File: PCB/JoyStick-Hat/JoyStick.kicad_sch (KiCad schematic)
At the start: 0 parts

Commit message: LED drivers and Joystick
Finished LED driver scheamtics, corrected some problems with symbols. added conenctors for joystick and buttons, connected RPI pins to MCU
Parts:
- added J4, J5: Conn_01x03_Pin, symbol Connector:Conn_01x03_Pin
- added J6: Conn_01x04_Pin, symbol Connector:Conn_01x04_Pin
- added J7, J8: Conn_01x02_Pin, symbol Connector:Conn_01x02_Pin
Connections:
- new net +3.3V: J4.3 (Pin_3), J5.3 (Pin_3)
- new net GND: J4.1 (Pin_1), J5.1 (Pin_1)
- new net JOYSTICK_X: J5.2 (Pin_2)
- new net JOYSTICK_Y: J4.2 (Pin_2)
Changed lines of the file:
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@@
 (kicad_sch (version 20230121) (generator eeschema)
   (paper "A4")
+  (wire (pts (xy 44.45 113.03) (xy 102.87 113.03))
+    (stroke (width 0) (type default))
+  )
+  (wire (pts (xy 102.87 115.57) (xy 102.87 124.46))
+    (stroke (width 0) (type default))
+  )
+  (wire (pts (xy 44.45 80.01) (xy 102.87 80.01))
+    (stroke (width 0) (type default))
+  )
+  (wire (pts (xy 102.87 68.58) (xy 102.87 77.47))
+    (stroke (width 0) (type default))
+  )
+  (wire (pts (xy 102.87 82.55) (xy 102.87 88.9))
+    (stroke (width 0) (type default))
+  )
+  (wire (pts (xy 102.87 102.87) (xy 102.87 110.49))
+    (stroke (width 0) (type default))
+  )
+  (hierarchical_label "JOYSTICK_X" (shape input) (at 44.45 80.01 180) (fields_autoplaced)
+    (effects (font (size 1.27 1.27)) (justify right))
+  )
+  (hierarchical_label "JOYSTICK_Y" (shape input) (at 44.45 113.03 180) (fields_autoplaced)
+    (effects (font (size 1.27 1.27)) (justify right))
+  )
+  (symbol (lib_id "Connector:Conn_01x02_Pin") (at 171.45 101.6 0) (unit 1)
+    (in_bom yes) (on_board yes) (dnp no)
+    (property "Reference" "J7" (at 172.72 99.06 0)
+      (effects (font (size 1.27 1.27)))
+    )
+    (property "Value" "Conn_01x02_Pin" (at 179.07 106.68 0)
+      (effects (font (size 1.27 1.27)))
+    )
+    (property "Footprint" "" (at 171.45 101.6 0)
+      (effects (font (size 1.27 1.27)) hide)
+    )
+    (property "Datasheet" "~" (at 171.45 101.6 0)
+      (effects (font (size 1.27 1.27)) hide)
+    )
+    (pin "1")
+    (pin "2")
+    (instances
+      (project "JoyStick-Hat"
+        (path "/cf0c81b5-5bdf-47c3-83c0-f6980f515e65/657fac1d-f0e2-4536-8020-58a2ff4b82f6"
+          (reference "J7") (unit 1)
+        )
+      )
+    )
+  )
+  (symbol (lib_id "Connector:Conn_01x02_Pin") (at 171.45 121.92 0) (unit 1)
+    (in_bom yes) (on_board yes) (dnp no)
+    (property "Reference" "J8" (at 172.72 119.38 0)
+      (effects (font (size 1.27 1.27)))
+    )
+    (property "Value" "Conn_01x02_Pin" (at 179.07 127 0)
+      (effects (font (size 1.27 1.27)))
+    )
+    (property "Footprint" "" (at 171.45 121.92 0)
+      (effects (font (size 1.27 1.27)) hide)
+    )
+    (property "Datasheet" "~" (at 171.45 121.92 0)
+      (effects (font (size 1.27 1.27)) hide)
+    )
+    (pin "1")
+    (pin "2")
+    (instances
+      (project "JoyStick-Hat"
+        (path "/cf0c81b5-5bdf-47c3-83c0-f6980f515e65/657fac1d-f0e2-4536-8020-58a2ff4b82f6"
+          (reference "J8") (unit 1)
+        )
+      )
+    )
+  )
+  (symbol (lib_id "Connector:Conn_01x03_Pin") (at 107.95 80.01 180) (unit 1)
+    (in_bom yes) (on_board yes) (dnp no) (fields_autoplaced)
+    (property "Reference" "J5" (at 109.22 78.74 0)
+      (effects (font (size 1.27 1.27)) (justify right))
+    )
+    (property "Value" "Conn_01x03_Pin" (at 109.22 81.28 0)
+      (effects (font (size 1.27 1.27)) (justify right))
+    )
+    (property "Footprint" "" (at 107.95 80.01 0)
+      (effects (font (size 1.27 1.27)) hide)
+    )
+    (property "Datasheet" "~" (at 107.95 80.01 0)
+      (effects (font (size 1.27 1.27)) hide)
+    )
+    (pin "1")
+    (pin "2")
+    (pin "3")
+    (instances
+      (project "JoyStick-Hat"
+        (path "/cf0c81b5-5bdf-47c3-83c0-f6980f515e65/657fac1d-f0e2-4536-8020-58a2ff4b82f6"
+          (reference "J5") (unit 1)
+        )
+      )
+    )
+  )
+  (symbol (lib_id "Connector:Conn_01x03_Pin") (at 107.95 113.03 180) (unit 1)
+    (in_bom yes) (on_board yes) (dnp no) (fields_autoplaced)
+    (property "Reference" "J4" (at 109.22 111.76 0)
+      (effects (font (size 1.27 1.27)) (justify right))
+    )
+    (property "Value" "Conn_01x03_Pin" (at 109.22 114.3 0)
+      (effects (font (size 1.27 1.27)) (justify right))
+    )
+    (property "Footprint" "" (at 107.95 113.03 0)
+      (effects (font (size 1.27 1.27)) hide)
+    )
+    (property "Datasheet" "~" (at 107.95 113.03 0)
+      (effects (font (size 1.27 1.27)) hide)
+    )
+    (pin "1")
+    (pin "2")
+    (pin "3")
+    (instances
+      (project "JoyStick-Hat"
+        (path "/cf0c81b5-5bdf-47c3-83c0-f6980f515e65/657fac1d-f0e2-4536-8020-58a2ff4b82f6"
+          (reference "J4") (unit 1)
+        )
+      )
+    )
+  )
+  (symbol (lib_id "power:GND") (at 102.87 124.46 0) (unit 1)
+    (in_bom yes) (on_board yes) (dnp no) (fields_autoplaced)
+    (property "Reference" "#PWR040" (at 102.87 130.81 0)
+      (effects (font (size 1.27 1.27)) hide)
+    )
+    (property "Value" "GND" (at 102.87 129.54 0)
+      (effects (font (size 1.27 1.27)))
+    )
+    (property "Footprint" "" (at 102.87 124.46 0)
+      (effects (font (size 1.27 1.27)) hide)
+    )
+    (property "Datasheet" "" (at 102.87 124.46 0)
+      (effects (font (size 1.27 1.27)) hide)
+    )
+    (pin "1")
+    (instances
+      (project "JoyStick-Hat"
+        (path "/cf0c81b5-5bdf-47c3-83c0-f6980f515e65/657fac1d-f0e2-4536-8020-58a2ff4b82f6"
+          (reference "#PWR040") (unit 1)
+        )
+      )
+    )
+  )
+  (symbol (lib_id "power:+3.3V") (at 102.87 102.87 0) (unit 1)
+    (in_bom yes) (on_board yes) (dnp no) (fields_autoplaced)
+    (property "Reference" "#PWR041" (at 102.87 106.68 0)
+      (effects (font (size 1.27 1.27)) hide)
+    )
+    (property "Value" "+3.3V" (at 102.87 97.79 0)
+      (effects (font (size 1.27 1.27)))
+    )
+    (property "Footprint" "" (at 102.87 102.87 0)
+      (effects (font (size 1.27 1.27)) hide)
+    )
+    (property "Datasheet" "" (at 102.87 102.87 0)
+      (effects (font (size 1.27 1.27)) hide)
+    )
+    (pin "1")
+    (instances
+      (project "JoyStick-Hat"
+        (path "/cf0c81b5-5bdf-47c3-83c0-f6980f515e65/657fac1d-f0e2-4536-8020-58a2ff4b82f6"
+          (reference "#PWR041") (unit 1)
+        )
+      )
+    )
+  )
+  (symbol (lib_id "Connector:Conn_01x04_Pin") (at 170.18 80.01 0) (unit 1)
+    (in_bom yes) (on_board yes) (dnp no)
+    (property "Reference" "J6" (at 170.18 74.93 0)
+      (effects (font (size 1.27 1.27)))
+    )
+    (property "Value" "Conn_01x04_Pin" (at 177.8 87.63 0)
+      (effects (font (size 1.27 1.27)))
+    )
+    (property "Footprint" "" (at 170.18 80.01 0)
+      (effects (font (size 1.27 1.27)) hide)
+    )
+    (property "Datasheet" "~" (at 170.18 80.01 0)
+      (effects (font (size 1.27 1.27)) hide)
+    )
+    (pin "1")
+    (pin "2")
+    (pin "3")
+    (pin "4")
+    (instances
+      (project "JoyStick-Hat"
+        (path "/cf0c81b5-5bdf-47c3-83c0-f6980f515e65/657fac1d-f0e2-4536-8020-58a2ff4b82f6"
+          (reference "J6") (unit 1)
+        )
+      )
+    )
+  )
+  (symbol (lib_id "power:GND") (at 102.87 88.9 0) (unit 1)
+    (in_bom yes) (on_board yes) (dnp no) (fields_autoplaced)
+    (property "Reference" "#PWR039" (at 102.87 95.25 0)
+      (effects (font (size 1.27 1.27)) hide)
+    )
+    (property "Value" "GND" (at 102.87 93.98 0)
+      (effects (font (size 1.27 1.27)))
+    )
+    (property "Footprint" "" (at 102.87 88.9 0)
+      (effects (font (size 1.27 1.27)) hide)
+    )
+    (property "Datasheet" "" (at 102.87 88.9 0)
+      (effects (font (size 1.27 1.27)) hide)
+    )
+    (pin "1")
+    (instances
+      (project "JoyStick-Hat"
+        (path "/cf0c81b5-5bdf-47c3-83c0-f6980f515e65/657fac1d-f0e2-4536-8020-58a2ff4b82f6"
+          (reference "#PWR039") (unit 1)
+        )
+      )
+    )
+  )
+  (symbol (lib_id "power:+3.3V") (at 102.87 68.58 0) (unit 1)
+    (in_bom yes) (on_board yes) (dnp no) (fields_autoplaced)
+    (property "Reference" "#PWR042" (at 102.87 72.39 0)
+      (effects (font (size 1.27 1.27)) hide)
+    )
+    (property "Value" "+3.3V" (at 102.87 63.5 0)
+      (effects (font (size 1.27 1.27)))
+    )
+    (property "Footprint" "" (at 102.87 68.58 0)
+      (effects (font (size 1.27 1.27)) hide)
+    )
+    (property "Datasheet" "" (at 102.87 68.58 0)
+      (effects (font (size 1.27 1.27)) hide)
+    )
+    (pin "1")
+    (instances
+      (project "JoyStick-Hat"
+        (path "/cf0c81b5-5bdf-47c3-83c0-f6980f515e65/657fac1d-f0e2-4536-8020-58a2ff4b82f6"
+          (reference "#PWR042") (unit 1)
+        )
+      )
+    )
+  )
 )

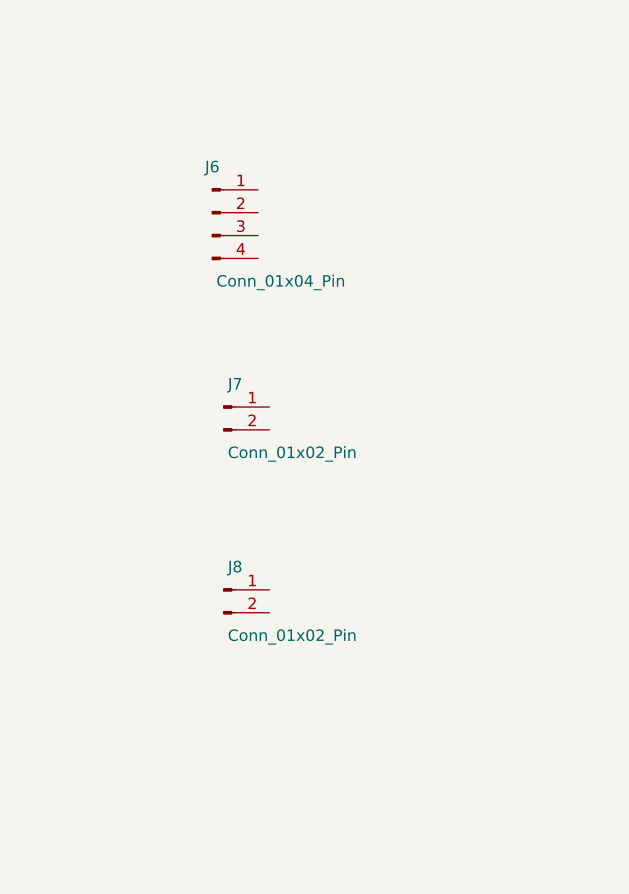
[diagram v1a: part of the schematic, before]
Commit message: Sheet Conenctivity and RS485
Added more sheet entries throughuot the project connecting different subsystems to the main MCU schematic. Also added  new sheet for the RS485 interface for communicating with the motor control board.
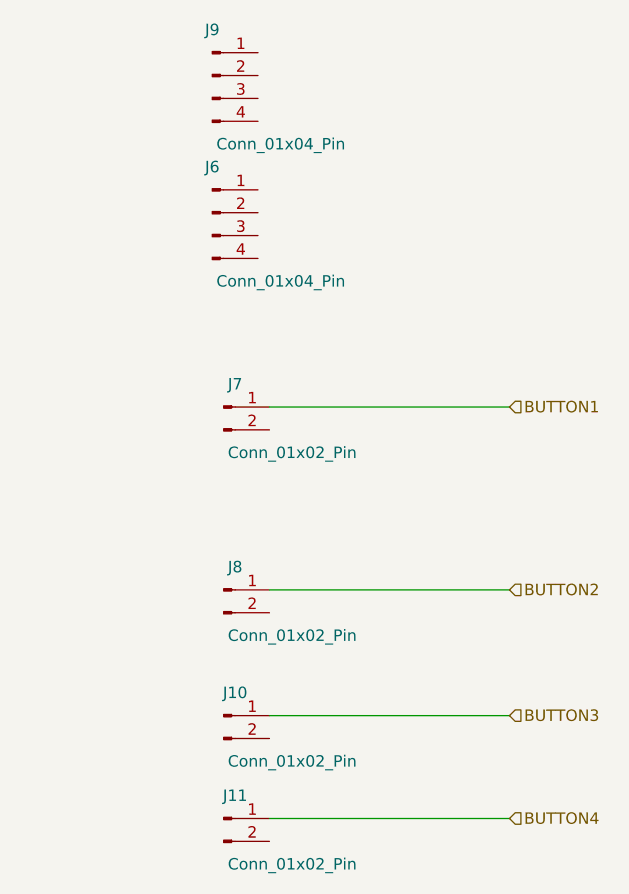
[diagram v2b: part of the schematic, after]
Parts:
- added J10, J11: Conn_01x02_Pin, symbol Connector:Conn_01x02_Pin
- added J9: Conn_01x04_Pin, symbol Connector:Conn_01x04_Pin
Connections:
- net BUTTON1: now reaches J7.1 (Pin_1)
- net BUTTON2: now reaches J8.1 (Pin_1)
- new net BUTTON3: J10.1 (Pin_1)
- new net BUTTON4: J11.1 (Pin_1)
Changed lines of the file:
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@@
 (kicad_sch (version 20230121) (generator eeschema)
   (paper "A4")
+  (wire (pts (xy 176.53 121.92) (xy 203.2 121.92))
+    (stroke (width 0) (type default))
+  )
   (wire (pts (xy 44.45 113.03) (xy 102.87 113.03))
     (stroke (width 0) (type default))
@@
     (stroke (width 0) (type default))
   )
+  (wire (pts (xy 176.53 101.6) (xy 203.2 101.6))
+    (stroke (width 0) (type default))
+  )
+  (wire (pts (xy 176.53 147.32) (xy 203.2 147.32))
+    (stroke (width 0) (type default))
+  )
   (wire (pts (xy 44.45 80.01) (xy 102.87 80.01))
     (stroke (width 0) (type default))
@@
   (wire (pts (xy 102.87 102.87) (xy 102.87 110.49))
     (stroke (width 0) (type default))
+  )
+  (wire (pts (xy 176.53 135.89) (xy 203.2 135.89))
+    (stroke (width 0) (type default))
+  )
+  (hierarchical_label "BUTTON3" (shape input) (at 203.2 135.89 0) (fields_autoplaced)
+    (effects (font (size 1.27 1.27)) (justify left))
+  )
+  (hierarchical_label "BUTTON2" (shape input) (at 203.2 121.92 0) (fields_autoplaced)
+    (effects (font (size 1.27 1.27)) (justify left))
   )
   (hierarchical_label "JOYSTICK_X" (shape input) (at 44.45 80.01 180) (fields_autoplaced)
@@
     (effects (font (size 1.27 1.27)) (justify right))
   )
+  (hierarchical_label "BUTTON1" (shape input) (at 203.2 101.6 0) (fields_autoplaced)
+    (effects (font (size 1.27 1.27)) (justify left))
+  )
+  (hierarchical_label "BUTTON4" (shape input) (at 203.2 147.32 0) (fields_autoplaced)
+    (effects (font (size 1.27 1.27)) (justify left))
+  )
   (symbol (lib_id "Connector:Conn_01x02_Pin") (at 171.45 101.6 0) (unit 1)
     (in_bom yes) (on_board yes) (dnp no)
@@
     )
   )
-  (symbol (lib_id "power:+3.3V") (at 102.87 102.87 0) (unit 1)
-    (in_bom yes) (on_board yes) (dnp no) (fields_autoplaced)
-    (property "Reference" "#PWR041" (at 102.87 106.68 0)
-      (effects (font (size 1.27 1.27)) hide)
-    )
-    (property "Value" "+3.3V" (at 102.87 97.79 0)
-      (effects (font (size 1.27 1.27)))
-    )
-    (property "Footprint" "" (at 102.87 102.87 0)
-      (effects (font (size 1.27 1.27)) hide)
-    )
-    (property "Datasheet" "" (at 102.87 102.87 0)
-      (effects (font (size 1.27 1.27)) hide)
-    )
-    (pin "1")
-    (instances
-      (project "JoyStick-Hat"
-        (path "/cf0c81b5-5bdf-47c3-83c0-f6980f515e65/657fac1d-f0e2-4536-8020-58a2ff4b82f6"
-          (reference "#PWR041") (unit 1)
-        )
-      )
-    )
-  )
-  (symbol (lib_id "Connector:Conn_01x04_Pin") (at 170.18 80.01 0) (unit 1)
-    (in_bom yes) (on_board yes) (dnp no)
-    (property "Reference" "J6" (at 170.18 74.93 0)
-      (effects (font (size 1.27 1.27)))
-    )
-    (property "Value" "Conn_01x04_Pin" (at 177.8 87.63 0)
-      (effects (font (size 1.27 1.27)))
-    )
-    (property "Footprint" "" (at 170.18 80.01 0)
-      (effects (font (size 1.27 1.27)) hide)
-    )
-    (property "Datasheet" "~" (at 170.18 80.01 0)
+  (symbol (lib_id "Connector:Conn_01x04_Pin") (at 170.18 64.77 0) (unit 1)
+    (in_bom yes) (on_board yes) (dnp no)
+    (property "Reference" "J9" (at 170.18 59.69 0)
+      (effects (font (size 1.27 1.27)))
+    )
+    (property "Value" "Conn_01x04_Pin" (at 177.8 72.39 0)
+      (effects (font (size 1.27 1.27)))
+    )
+    (property "Footprint" "" (at 170.18 64.77 0)
+      (effects (font (size 1.27 1.27)) hide)
+    )
+    (property "Datasheet" "~" (at 170.18 64.77 0)
       (effects (font (size 1.27 1.27)) hide)
     )
@@
       (project "JoyStick-Hat"
         (path "/cf0c81b5-5bdf-47c3-83c0-f6980f515e65/657fac1d-f0e2-4536-8020-58a2ff4b82f6"
+          (reference "J9") (unit 1)
+        )
+      )
+    )
+  )
+  (symbol (lib_id "Connector:Conn_01x02_Pin") (at 171.45 135.89 0) (unit 1)
+    (in_bom yes) (on_board yes) (dnp no)
+    (property "Reference" "J10" (at 172.72 133.35 0)
+      (effects (font (size 1.27 1.27)))
+    )
+    (property "Value" "Conn_01x02_Pin" (at 179.07 140.97 0)
+      (effects (font (size 1.27 1.27)))
+    )
+    (property "Footprint" "" (at 171.45 135.89 0)
+      (effects (font (size 1.27 1.27)) hide)
+    )
+    (property "Datasheet" "~" (at 171.45 135.89 0)
+      (effects (font (size 1.27 1.27)) hide)
+    )
+    (pin "1")
+    (pin "2")
+    (instances
+      (project "JoyStick-Hat"
+        (path "/cf0c81b5-5bdf-47c3-83c0-f6980f515e65/657fac1d-f0e2-4536-8020-58a2ff4b82f6"
+          (reference "J10") (unit 1)
+        )
+      )
+    )
+  )
+  (symbol (lib_id "power:+3.3V") (at 102.87 102.87 0) (unit 1)
+    (in_bom yes) (on_board yes) (dnp no) (fields_autoplaced)
+    (property "Reference" "#PWR041" (at 102.87 106.68 0)
+      (effects (font (size 1.27 1.27)) hide)
+    )
+    (property "Value" "+3.3V" (at 102.87 97.79 0)
+      (effects (font (size 1.27 1.27)))
+    )
+    (property "Footprint" "" (at 102.87 102.87 0)
+      (effects (font (size 1.27 1.27)) hide)
+    )
+    (property "Datasheet" "" (at 102.87 102.87 0)
+      (effects (font (size 1.27 1.27)) hide)
+    )
+    (pin "1")
+    (instances
+      (project "JoyStick-Hat"
+        (path "/cf0c81b5-5bdf-47c3-83c0-f6980f515e65/657fac1d-f0e2-4536-8020-58a2ff4b82f6"
+          (reference "#PWR041") (unit 1)
+        )
+      )
+    )
+  )
+  (symbol (lib_id "Connector:Conn_01x04_Pin") (at 170.18 80.01 0) (unit 1)
+    (in_bom yes) (on_board yes) (dnp no)
+    (property "Reference" "J6" (at 170.18 74.93 0)
+      (effects (font (size 1.27 1.27)))
+    )
+    (property "Value" "Conn_01x04_Pin" (at 177.8 87.63 0)
+      (effects (font (size 1.27 1.27)))
+    )
+    (property "Footprint" "" (at 170.18 80.01 0)
+      (effects (font (size 1.27 1.27)) hide)
+    )
+    (property "Datasheet" "~" (at 170.18 80.01 0)
+      (effects (font (size 1.27 1.27)) hide)
+    )
+    (pin "1")
+    (pin "2")
+    (pin "3")
+    (pin "4")
+    (instances
+      (project "JoyStick-Hat"
+        (path "/cf0c81b5-5bdf-47c3-83c0-f6980f515e65/657fac1d-f0e2-4536-8020-58a2ff4b82f6"
           (reference "J6") (unit 1)
         )
@@
         )
       )
+    )
+  )
+  (symbol (lib_id "Connector:Conn_01x02_Pin") (at 171.45 147.32 0) (unit 1)
+    (in_bom yes) (on_board yes) (dnp no)
+    (property "Reference" "J11" (at 172.72 144.78 0)
+      (effects (font (size 1.27 1.27)))
+    )
+    (property "Value" "Conn_01x02_Pin" (at 179.07 152.4 0)
+      (effects (font (size 1.27 1.27)))
+    )
+    (property "Footprint" "" (at 171.45 147.32 0)
+      (effects (font (size 1.27 1.27)) hide)
+    )
+    (property "Datasheet" "~" (at 171.45 147.32 0)
+      (effects (font (size 1.27 1.27)) hide)
+    )
+    (pin "1")
+    (pin "2")
+    (instances
+      (project "JoyStick-Hat"
+        (path "/cf0c81b5-5bdf-47c3-83c0-f6980f515e65/657fac1d-f0e2-4536-8020-58a2ff4b82f6"
+          (reference "J11") (unit 1)
+        )
+      )
